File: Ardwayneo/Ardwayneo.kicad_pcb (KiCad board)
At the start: 2 copper layers, 17 parts, among them J1 Digital Pins, J2 ICSP, J3 Serial, J4 I2C, U1 24LC1025, U2 24LC1025, U3 ATMEGA328P-AU, U3 DS1337S+, Y1 Crystal 32MHz, Y2 Crystal 16MHz

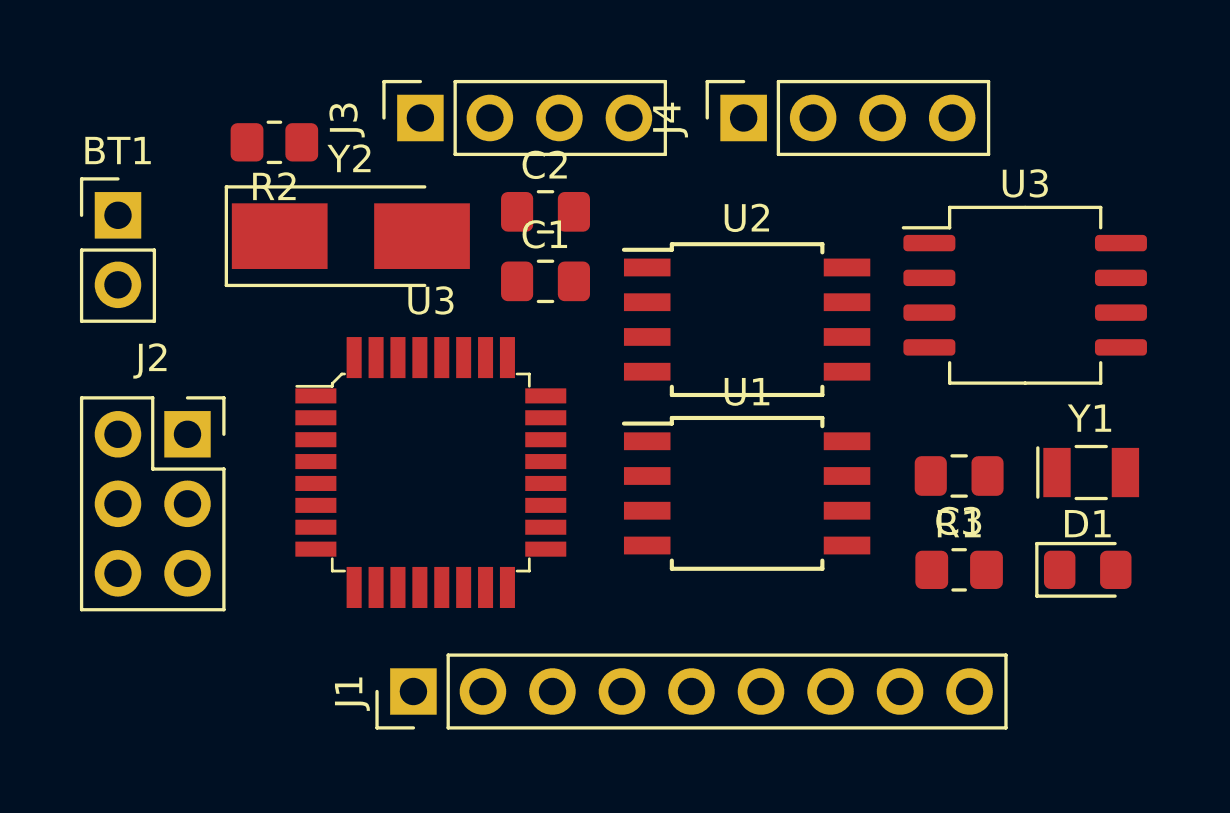
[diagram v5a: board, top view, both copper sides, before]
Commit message: added, rounded border boundary
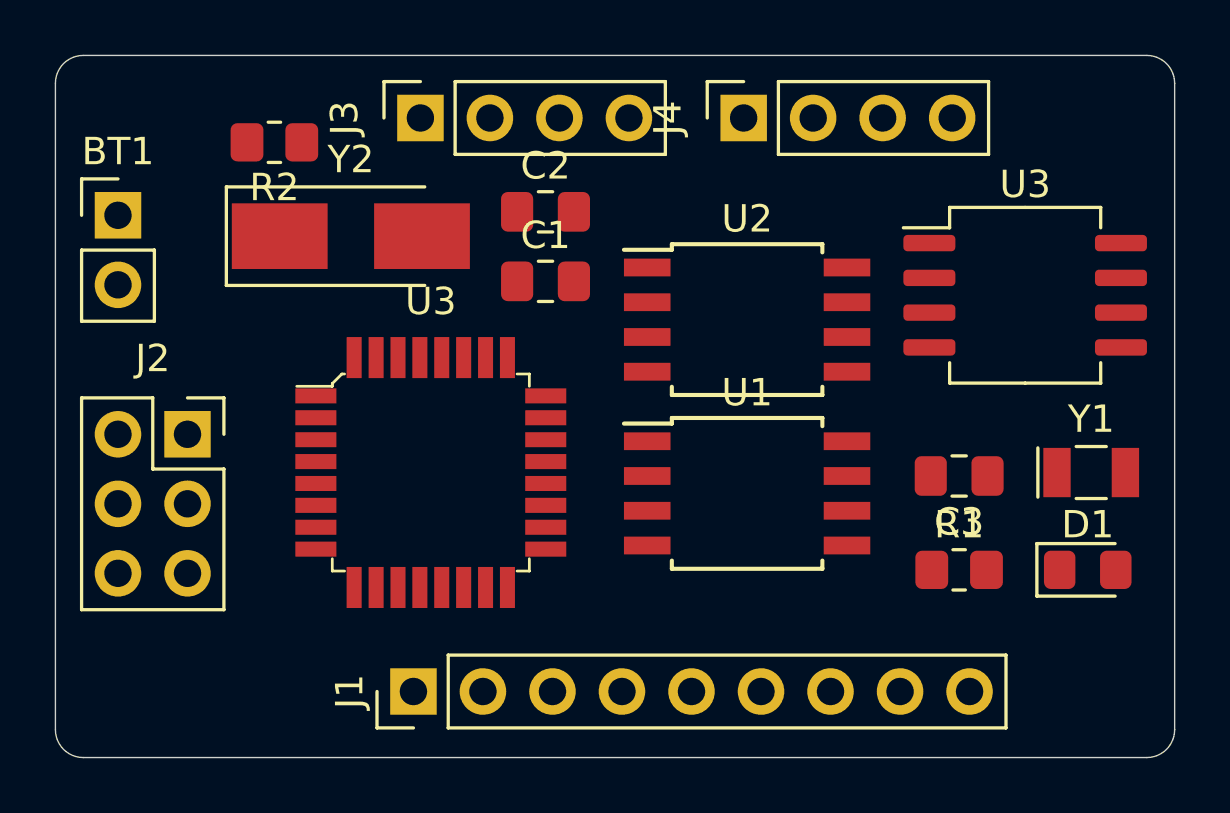
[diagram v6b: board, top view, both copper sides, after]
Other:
- board outline added: 40.9 x 25.7 mm
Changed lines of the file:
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@@
   (general
     (thickness 1.6)
-    (drawings 0)
+    (drawings 8)
     (tracks 0)
     (zones 0)
@@
     )
   )
+  (gr_line (start 125.222 104.902) (end 125.222 81.28) (layer Edge.Cuts) (width 0.05))
+  (gr_line (start 85.344 105.918) (end 124.206 105.918) (layer Edge.Cuts) (width 0.05))
+  (gr_line (start 84.328 81.28) (end 84.328 104.902) (layer Edge.Cuts) (width 0.05))
+  (gr_line (start 124.206 80.264) (end 85.344 80.264) (layer Edge.Cuts) (width 0.05))
+  (gr_arc (start 124.206 104.902) (end 124.206 105.918) (angle -90) (layer Edge.Cuts) (width 0.05))
+  (gr_arc (start 85.344 104.902) (end 84.328 104.902) (angle -90) (layer Edge.Cuts) (width 0.05))
+  (gr_arc (start 85.344 81.28) (end 85.344 80.264) (angle -90) (layer Edge.Cuts) (width 0.05))
+  (gr_arc (start 124.206 81.28) (end 125.222 81.28) (angle -90) (layer Edge.Cuts) (width 0.05))
 )

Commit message: Added mounting holes 4 corners
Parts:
- moved BT1 0.72 mm to (87.1, 86.6)
- moved J2 0.52 mm to (89.7, 94.0)
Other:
- outline, holes or cut-outs redrawn
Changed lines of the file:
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@@
   (general
     (thickness 1.6)
-    (drawings 8)
+    (drawings 12)
     (tracks 0)
     (zones 0)
@@
   )
   (module Connector_PinHeader_2.54mm:PinHeader_1x02_P2.54mm_Vertical (layer F.Cu)
-    (at 86.614 86.106)
+    (at 87.122 86.614)
     (descr "Through hole straight pin header, 1x02, 2.54mm pitch, single row")
     (tags "Through hole pin header THT 1x02 2.54mm single row")
@@
   )
   (module Connector_PinSocket_2.54mm:PinSocket_2x03_P2.54mm_Vertical (layer F.Cu)
-    (at 89.154 94.107)
+    (at 89.662 93.98)
     (descr "Through hole straight socket strip, 2x03, 2.54mm pitch, double cols (from Kicad 4.0.7), script generated")
     (tags "Through hole socket strip THT 2x03 2.54mm double row")
@@
     )
   )
+  (gr_circle (center 123.19 103.886) (end 123.952 104.394) (layer Edge.Cuts) (width 0.05))
+  (gr_circle (center 86.36 103.886) (end 87.122 103.378) (layer Edge.Cuts) (width 0.05))
+  (gr_circle (center 123.19 82.296) (end 123.952 81.788) (layer Edge.Cuts) (width 0.05))
+  (gr_circle (center 86.36 82.296) (end 86.868 81.534) (layer Edge.Cuts) (width 0.05))
   (gr_line (start 125.222 104.902) (end 125.222 81.28) (layer Edge.Cuts) (width 0.05))
   (gr_line (start 85.344 105.918) (end 124.206 105.918) (layer Edge.Cuts) (width 0.05))

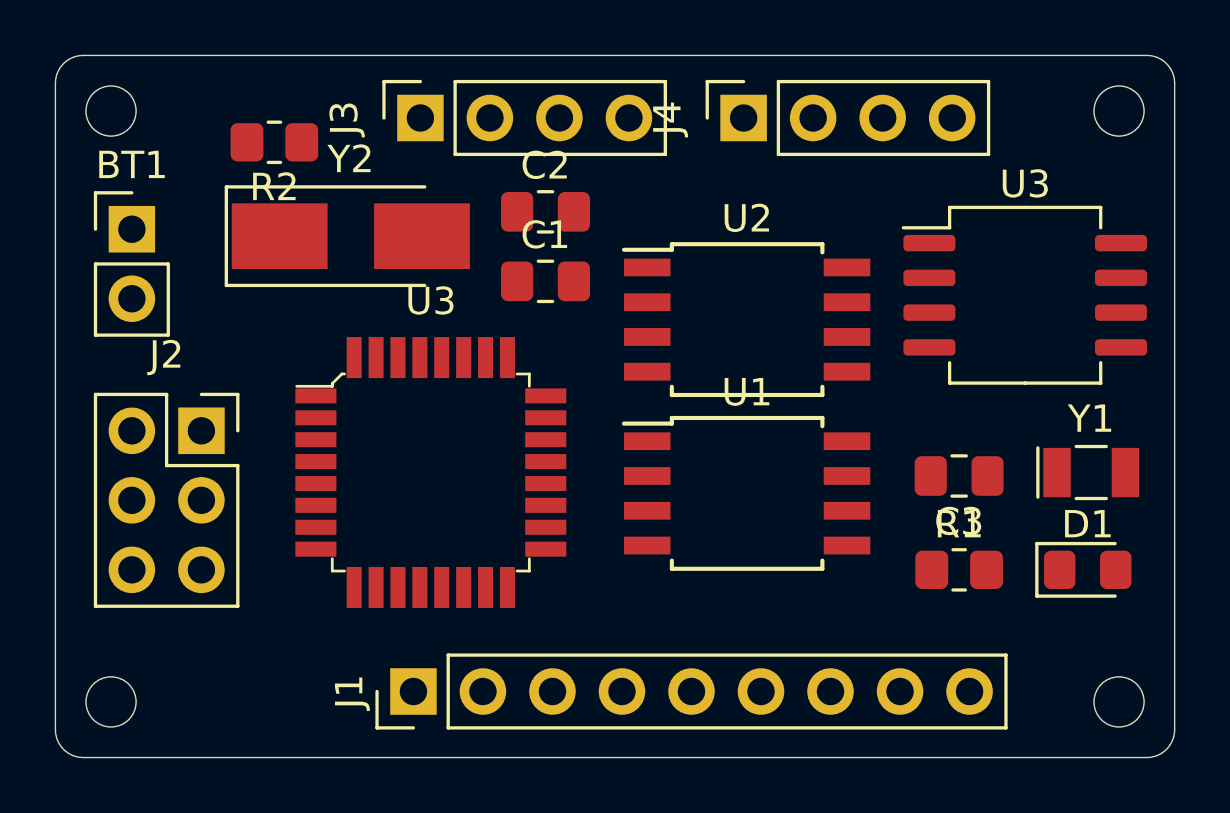
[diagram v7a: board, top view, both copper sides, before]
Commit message: Used 3rd pty autorouter, DRC checks out.
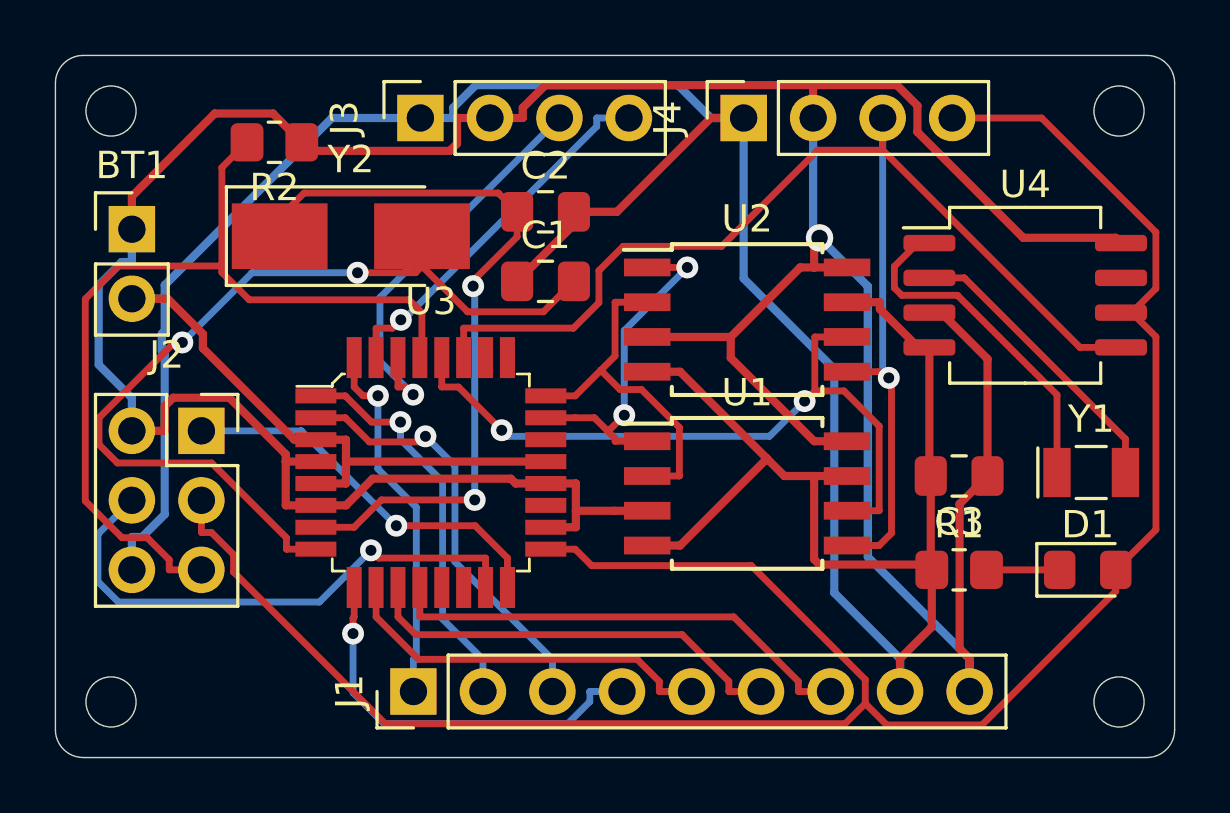
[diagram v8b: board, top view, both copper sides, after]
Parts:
- R1: value 330Ω -> 330ohm
- R2: value 10KΩ -> 10K
- renumbered U3 to U4
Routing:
- net /Vcc: track 0.00 -> 135.2 mm, vias 0 -> 1
- net GNDPWR: track 0.00 -> 130.8 mm
- net /SCK: track 0.00 -> 79.0 mm
- net /SDA: track 0.00 -> 51.4 mm, vias 0 -> 1
- net /RESET: track 0.00 -> 33.1 mm
- net Net-(C1-Pad2): track 0.00 -> 32.6 mm, vias 0 -> 2
- net Net-(C2-Pad1): track 0.00 -> 27.4 mm, vias 0 -> 2
- net /SCL: track 0.00 -> 26.4 mm, vias 0 -> 2
- net /MOSI: track 0.00 -> 19.9 mm, vias 0 -> 1
- net /D8: track 0.00 -> 17.4 mm
- net /D4: track 0.00 -> 15.7 mm, vias 0 -> 1
- net /D7: track 0.00 -> 15.7 mm
- net /RX: track 0.00 -> 15.1 mm, vias 0 -> 1
- net /D5: track 0.00 -> 14.9 mm, vias 0 -> 1
- net /D3: track 0.00 -> 14.6 mm, vias 0 -> 1
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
